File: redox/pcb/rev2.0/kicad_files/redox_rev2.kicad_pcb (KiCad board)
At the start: 2 copper layers, 162.2 x 138.8 mm, 150 parts, among them J1 AVR-ISP-6, J2 OLED-SSD1306, K1 KEYSW, K10 KEYSW, K11 KEYSW, K12 KEYSW, K13 KEYSW, K14 KEYSW, K15 KEYSW, K16 KEYSW, K17 KEYSW, K18 KEYSW, K19 KEYSW, K2 KEYSW, K20 KEYSW, K21 KEYSW, K22 KEYSW, K23 KEYSW, K24 KEYSW, K25 KEYSW, K26 KEYSW, K27 KEYSW, K28 KEYSW, K29 KEYSW, K3 KEYSW, K30 KEYSW, K31 KEYSW, K32 KEYSW, K33 KEYSW, K34 KEYSW, K35 KEYSW, K4 KEYSW, K5 KEYSW, K6 KEYSW, K7 KEYSW, K8 KEYSW, K9 KEYSW, Q1 2N7002, U1 PRTR5V0U2X, U2 ATmega32U4, Y1 16Mhz

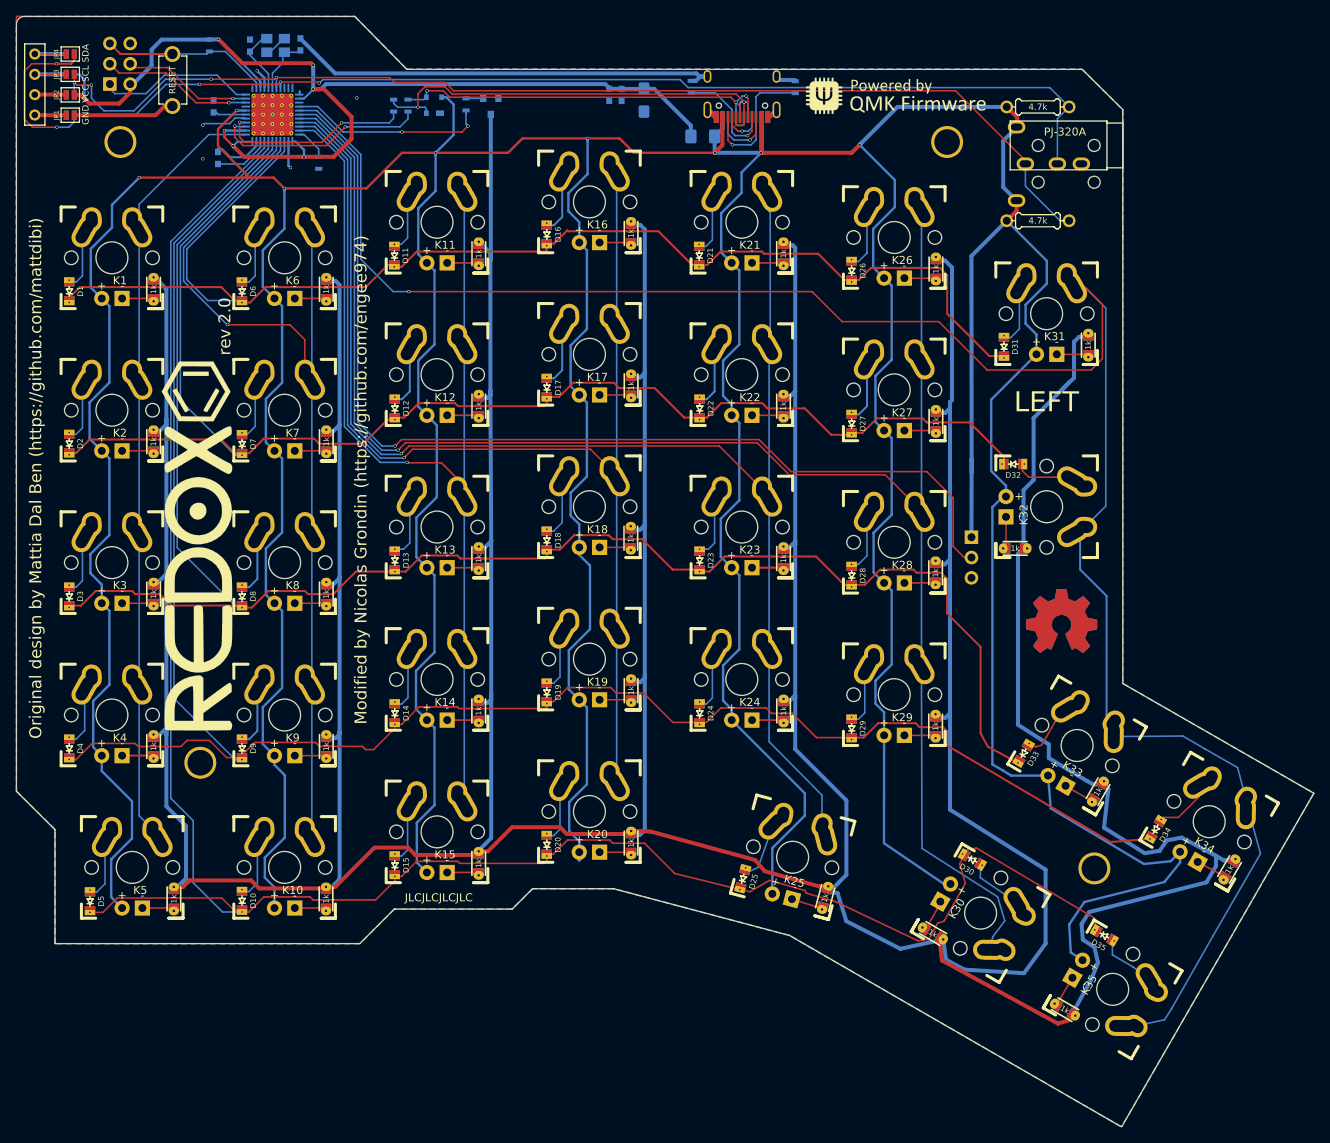
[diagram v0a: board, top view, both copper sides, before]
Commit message: Add holes for OLED cover and moove mounting holes
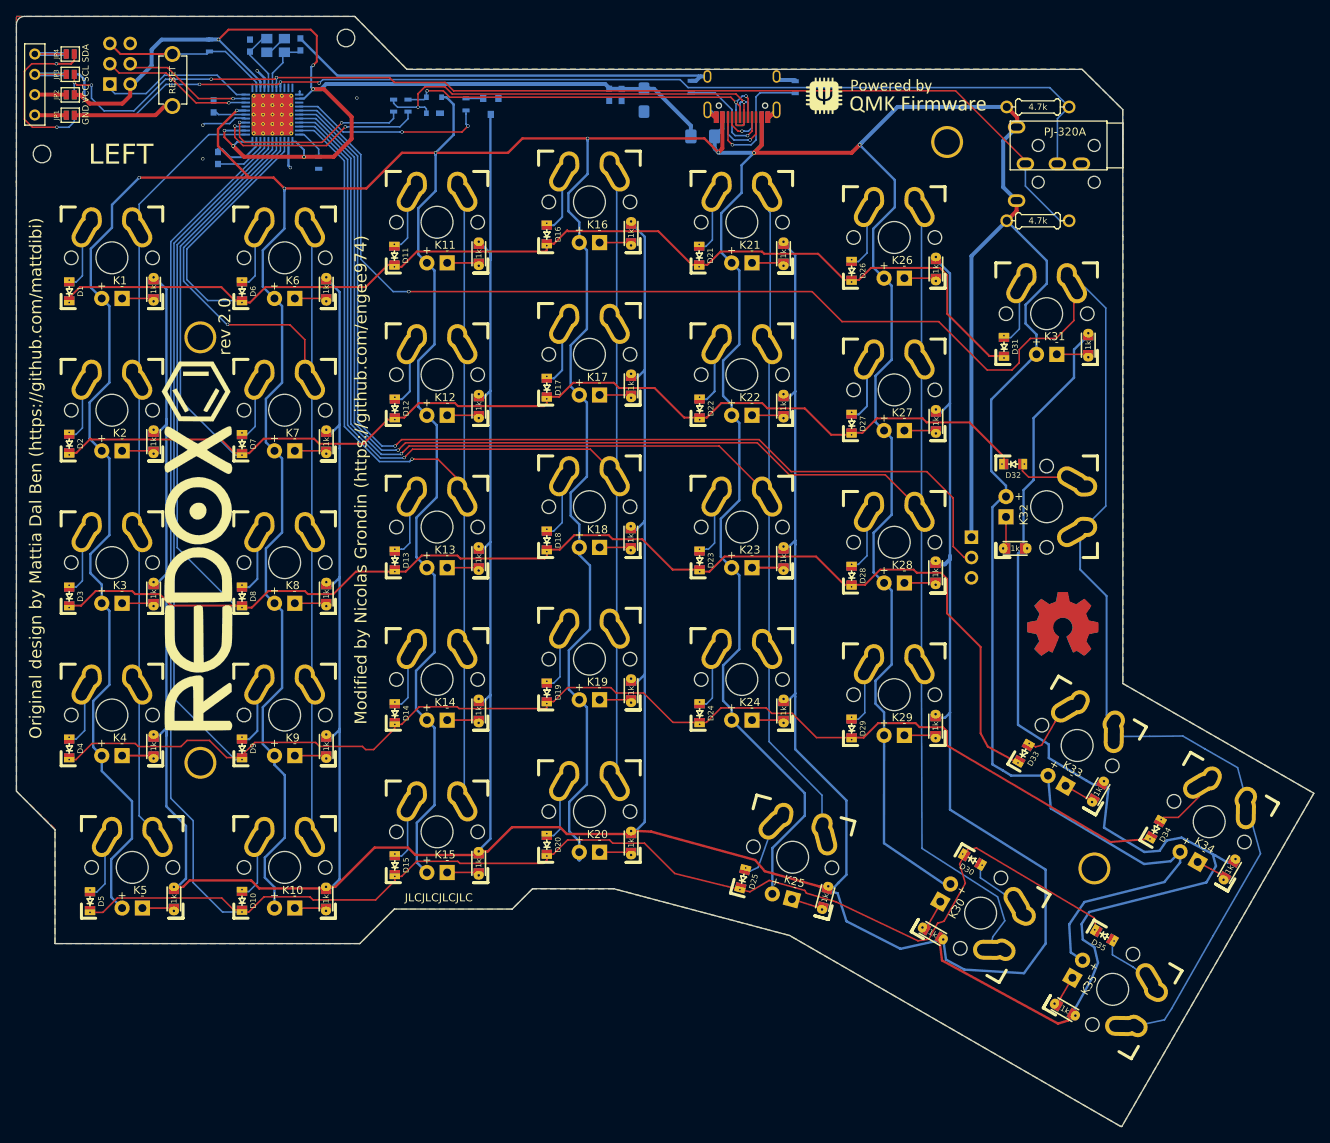
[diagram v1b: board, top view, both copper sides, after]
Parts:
- removed the REF** at (210.2, 112.1) (x2)
- added H5: MountingHole, redox_footprints:HOLE_M2, F.Cu at (82.7, 54.3)
- added H6: MountingHole, redox_footprints:HOLE_M2, F.Cu at (120.6, 39.4)
- added REF**: OSHW-Symbol_8.9x8mm_Copper, redox_footprints:OSHW-Symbol_8.9x8mm_Copper, B.Cu at (210.3, 112.5)
- added REF**: OSHW-Symbol_8.9x8mm_Copper, redox_footprints:OSHW-Symbol_8.9x8mm_Copper, F.Cu at (210.3, 112.5)
- moved H2 26.4 mm to (102.6, 77.5)
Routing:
- net LEDGND: track 826.2 -> 817.9 mm
- net col6: track 246.1 -> 238.4 mm
- net +5V: track 141.3 -> 145.6 mm
- net VCC: track 955.6 -> 954.4 mm
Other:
- net class GND: trace_width 0.3 -> 0.5
- net class VCC: trace_width 0.3 -> 0.5
- rule via_min_size: 0.3 -> 0.4

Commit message: Move mounting holes to be compliant with redox rev1
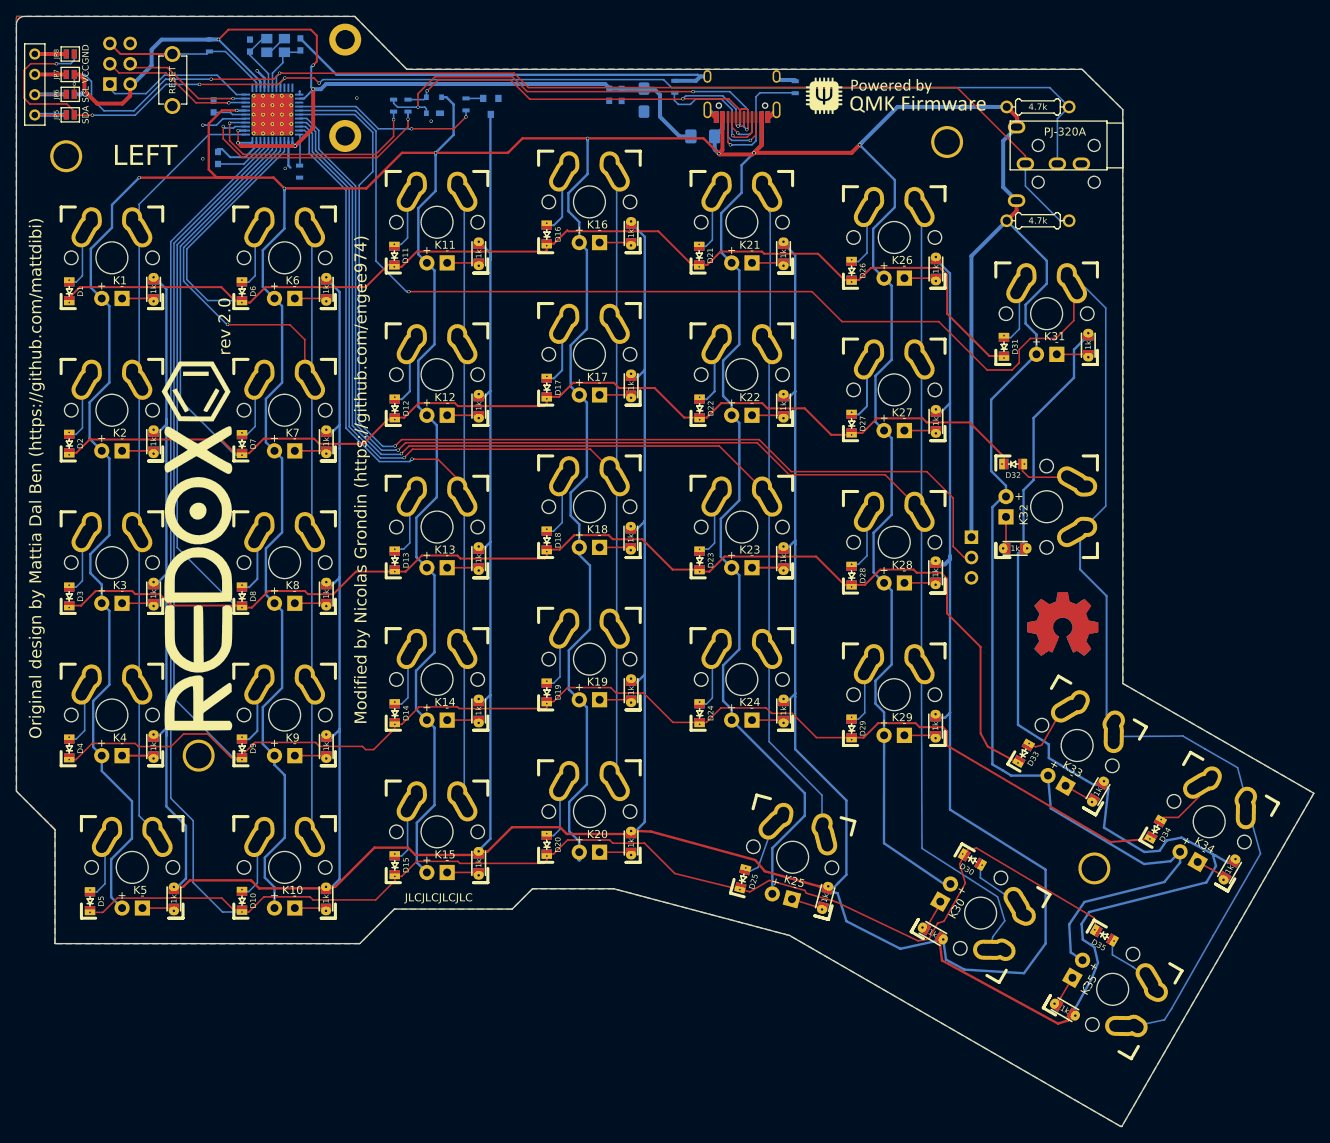
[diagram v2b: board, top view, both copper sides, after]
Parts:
- removed J1: AVR-ISP-6, Connector_PinHeader_2.54mm:PinHeader_2x03_P2.54mm_Vertical
- added P1: TC2030-AVR, Connector_PinHeader_2.54mm:PinHeader_2x03_P2.54mm_Vertical, B.Cu at (91.2, 45.0)
- H5, H6: footprint redox_footprints:HOLE_M2 -> redox_footprints:M2_HOLE_PCB
- JP1, JP2, JP3, JP4: moved to B.Cu
- JP5, JP6, JP7, JP8: moved to F.Cu
- moved H5 37.9 mm to (120.5, 51.5)
- moved R8 2.63 mm to (114.9, 55.9)
- moved R1 2.05 mm to (161.8, 45.3)
- moved H3 0.25 mm to (102.2, 129.8)
- moved JP2 0.07 mm to (86.2, 46.2)
- moved JP6 0.07 mm to (86.2, 46.2)
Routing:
- net +5V: track 145.6 -> 129.9 mm
- net GND: track 96.8 -> 87.0 mm, vias 5 -> 6
- net Net-(R4-Pad2): track 53.6 -> 60.1 mm
- net D+: track 24.2 -> 29.4 mm
- net VCC: track 954.4 -> 959.4 mm
- net D-: track 27.1 -> 32.0 mm
- net rgb_data: track 130.6 -> 134.9 mm
- net Net-(R1-Pad2): track 13.5 -> 17.1 mm
- net SCL: track 141.6 -> 143.7 mm, vias 4 -> 3
- net col6: track 238.4 -> 240.2 mm
- net SDA: track 157.5 -> 156.0 mm
- net Net-(R9-Pad2): track 24.7 -> 23.4 mm
- net Net-(USB1-Pad9): track 5.30 -> 6.12 mm
- net col3: track 148.4 -> 147.7 mm
- net row3: track 239.7 -> 240.4 mm
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
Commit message: Schematic correction : replace VCC by VBUS and +5V by VCC, some other minor changes
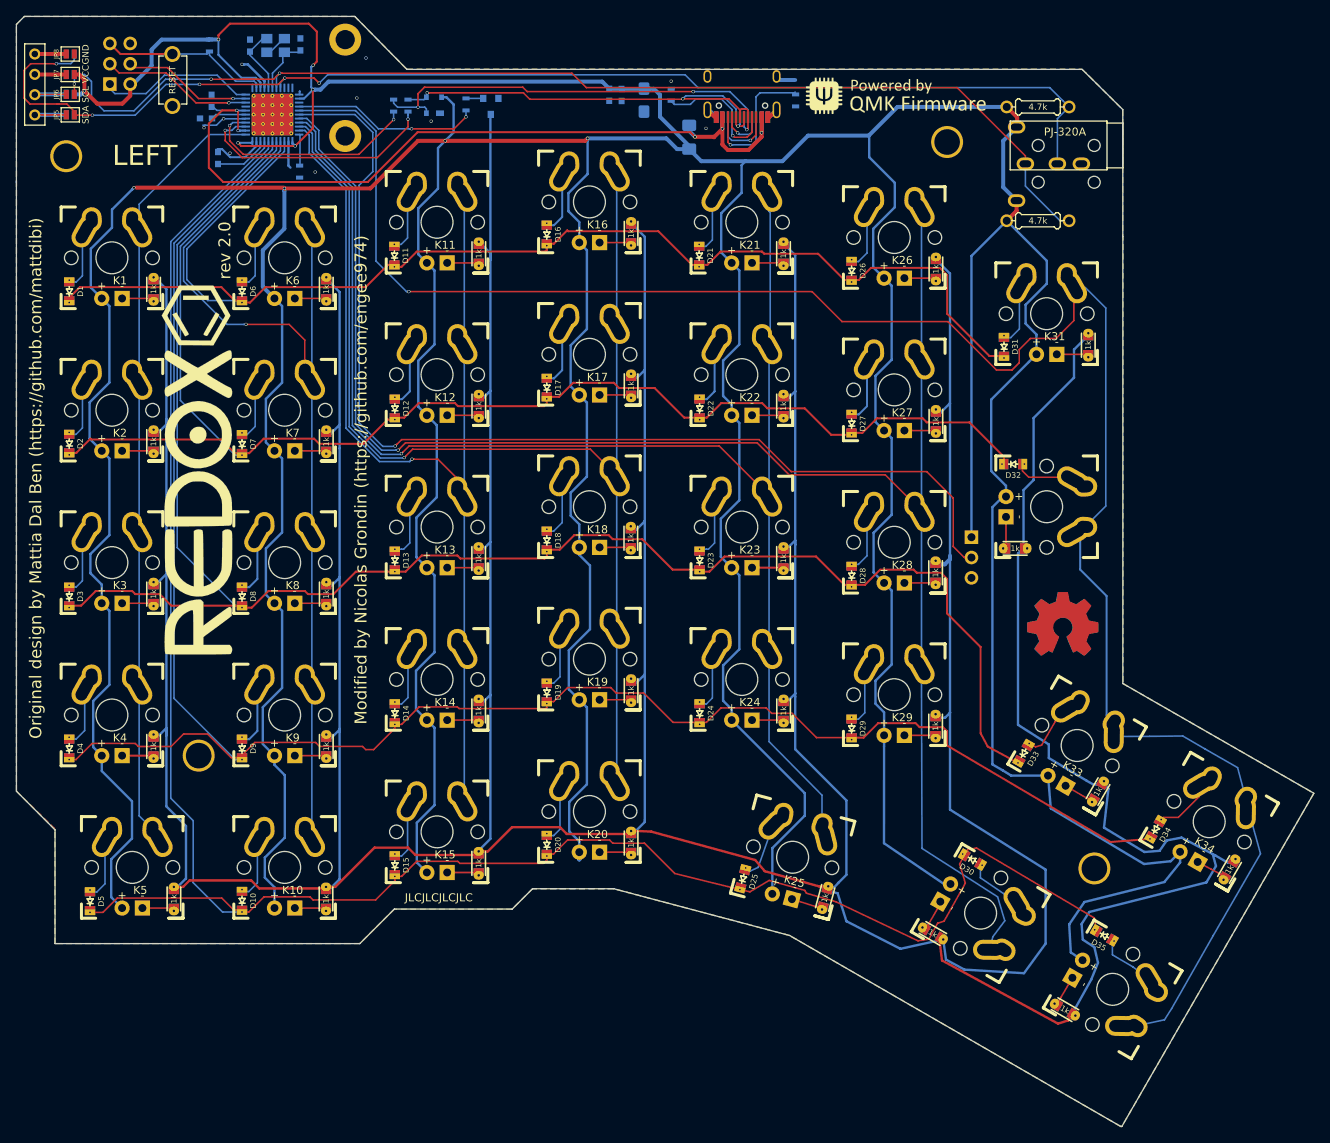
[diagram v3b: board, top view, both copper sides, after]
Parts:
- added C8: 1uF, Keebio-Parts:C_0603, B.Cu at (103.9, 47.0)
- K30, K32, K35: footprint redox_footprints:Mx_Alps_125-dualside_with_LED -> redox_footprints:Mx_Alps_150-dualsided_with_LED
- moved REDOX_BOTTOM 9.50 mm to (102.2, 93.2)
- moved REDOX_FRONT 9.50 mm to (102.2, 93.2)
- moved C4 1.77 mm to (103.2, 49.2), turned to 0 degrees
- moved F1 1.70 mm to (163.6, 51.6), turned to 90 degrees
- moved R2 1.65 mm to (176.9, 47.0), turned to 90 degrees
- moved R1 1.10 mm to (161.3, 46.3)
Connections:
- C5 pad 1: +5V -> VCC
- C6 pad 2: +5V -> VCC
- C7 pad 2: +5V -> VCC
- F1 pad 1: +5V -> VCC
- F1 pad 2: VCC -> VBUS
- JP2 pad 2: +5V -> VCC
- JP7 pad 2: +5V -> VCC
- P1 pad 2: +5V -> VCC
- R7 pad 1: +5V -> VCC
- U2 pad 14: +5V -> VCC
- U2 pad 2: +5V -> VBUS
- U2 pad 24: +5V -> VCC
- U2 pad 34: +5V -> VCC
- U2 pad 44: +5V -> VCC
- U2 pad 7: VCC -> VBUS
- USB1 pad 11: VCC -> VBUS
- USB1 pad 2: VCC -> VBUS
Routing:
- net +5V: track 129.9 -> 0.00 mm, vias 7 -> 0
- net VBUS: track 0.00 -> 102.4 mm, vias 0 -> 5
- net VCC: track 959.4 -> 1052.2 mm, vias 8 -> 10
- net GND: track 87.0 -> 31.9 mm, vias 6 -> 10
- net Net-(R4-Pad2): track 60.1 -> 58.6 mm
- net D+: track 29.4 -> 28.0 mm
- net Net-(R3-Pad2): track 58.8 -> 57.8 mm
- net D-: track 32.0 -> 31.2 mm
- net Net-(R1-Pad2): track 17.1 -> 16.6 mm
